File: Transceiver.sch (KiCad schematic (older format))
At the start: 31 parts

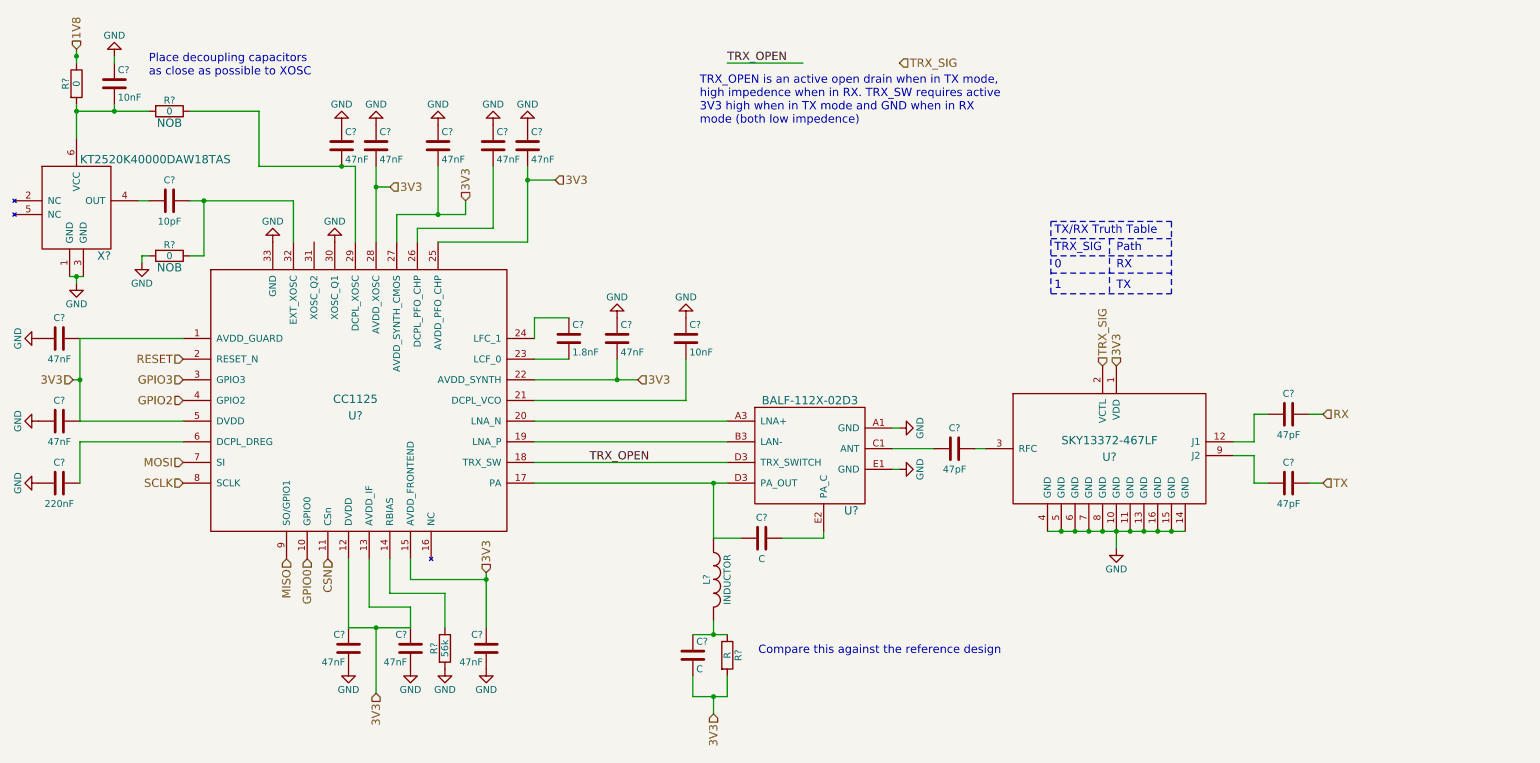
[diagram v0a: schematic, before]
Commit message: added jumpers for regulater EN and a jumper for fixing PA_ADJ. Connceted TRX_SIG to GPIO0
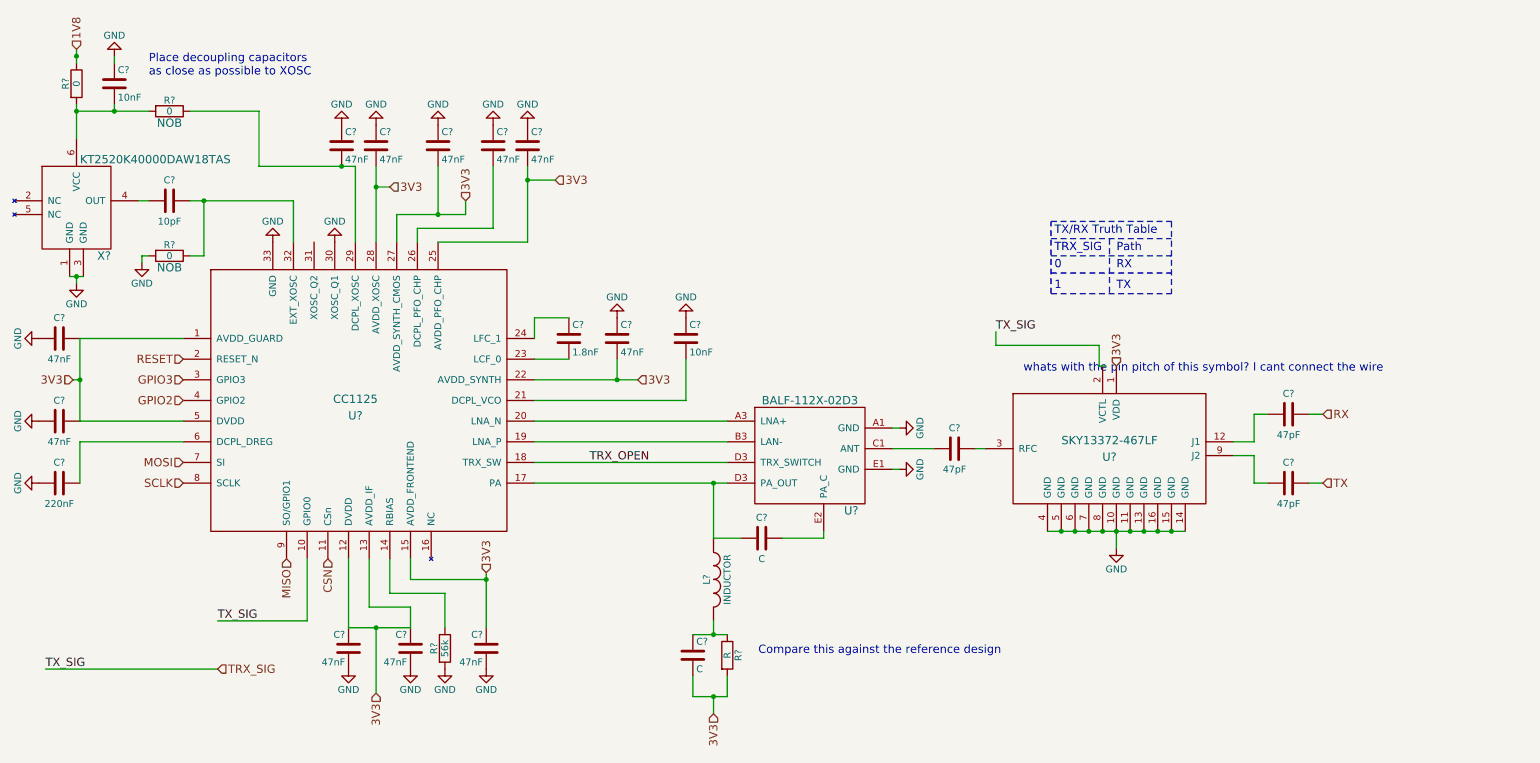
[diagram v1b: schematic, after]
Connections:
- net GPIO0 is gone; now on net TRX_SIG: U?.10 (GPIO0)
- net TRX_SIG: no longer U?.2 (VCTL)
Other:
- note added: "whats with the pin pitch of this symbol? I cant connect the wire\n"
- note removed: "TRX_OPEN is an active open drain when in TX mode, \nhigh impedence when in RX. TRX_SW requires active \n3V3 high when in TX mode and GND when in RX \nmode (both low impedence)"
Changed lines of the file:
@@
 Text HLabel 2550 4600 3    60   Input ~ 0
 MISO
-Text HLabel 2700 4600 3    60   Input ~ 0
-GPIO0
 Text HLabel 2850 4600 3    60   Input ~ 0
 CSN
@@
 Text HLabel 4500 1850 2    60   Input ~ 0
 3V3
-Text HLabel 7000 1000 2    60   Input ~ 0
+Text HLabel 2050 5400 2    60   Input ~ 0
 TRX_SIG
 $Comp
@@
 Text Label 4750 3900 0    60   ~ 0
 TRX_OPEN
-Text Label 5750 1000 0    60   ~ 0
-TRX_OPEN
+Text Label 800  5400 0    60   ~ 0
+TX_SIG
 Text HLabel 5650 5725 3    60   Input ~ 0
 3V3
-Text Notes 5550 1450 0    60   ~ 0
-TRX_OPEN is an active open drain when in TX mode, \nhigh impedence when in RX. TRX_SW requires active \n3V3 high when in TX mode and GND when in RX \nmode (both low impedence)
 Text Notes 1550 1100 0    60   ~ 0
 Place decoupling capacitors\nas close as possible to XOSC\n
@@
 	0    1    1    0
 $EndComp
-Text HLabel 8475 3200 1    60   Input ~ 0
-TRX_SIG
 Text Notes 8125 2375 0    60   ~ 0
 TRX_SIG
@@
 Connection ~ 3200 5100
 Wire Wire Line
-	5750 1000 6300 1000
+	800  5400 2050 5400
 Wire Wire Line
 	5750 5600 5750 5450
@@
 Wire Wire Line
 	2350 1350 1850 1350
+Wire Wire Line
+	2700 4600 2700 5050
+Wire Wire Line
+	2700 5050 2050 5050
+Text Label 2050 5050 0    60   ~ 0
+TX_SIG
+Text Label 7700 2950 0    60   ~ 0
+TX_SIG
+Wire Wire Line
+	8500 3200 8450 3200
+Wire Wire Line
+	8450 3200 8450 3050
+Wire Wire Line
+	8450 3050 7700 3050
+Wire Wire Line
+	7700 3050 7700 2950
+Text Notes 7900 3250 0    60   ~ 0
+whats with the pin pitch of this symbol? I cant connect the wire\n
 $EndSCHEMATC

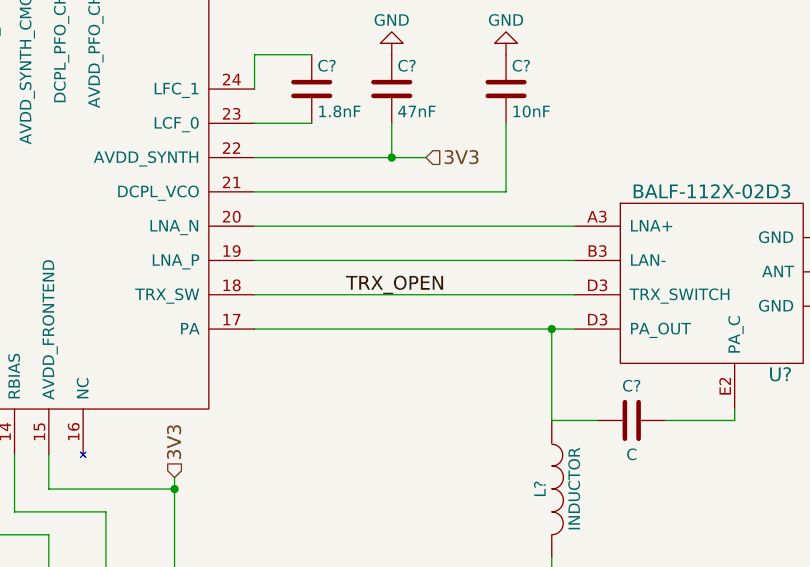
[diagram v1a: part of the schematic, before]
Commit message: deleted TRX_OPEN net
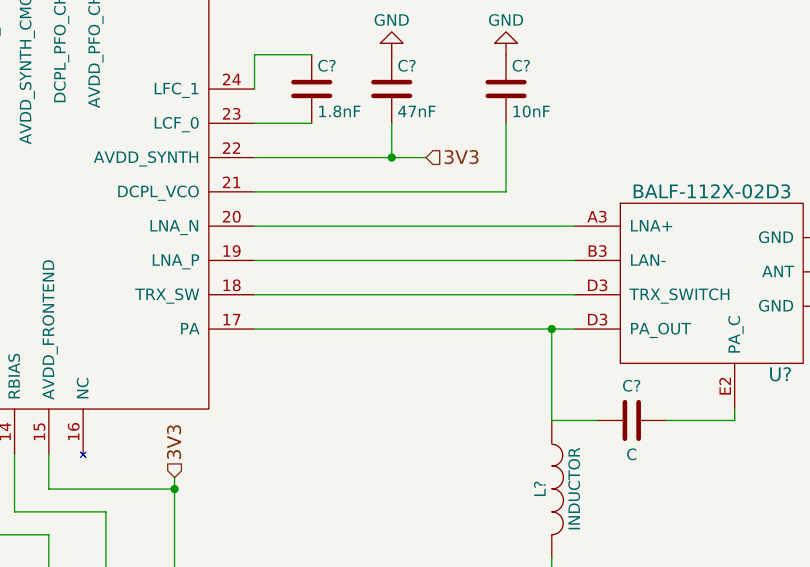
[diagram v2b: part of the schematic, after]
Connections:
- net TRX_OPEN: no longer names the net of U?.18 (TRX_SW), U?.D3 (TRX_SWITCH)
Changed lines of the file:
@@
 Text HLabel 5100 3300 2    60   Input ~ 0
 3V3
-Text Label 4750 3900 0    60   ~ 0
-TRX_OPEN
 Text Label 800  5400 0    60   ~ 0
 TX_SIG

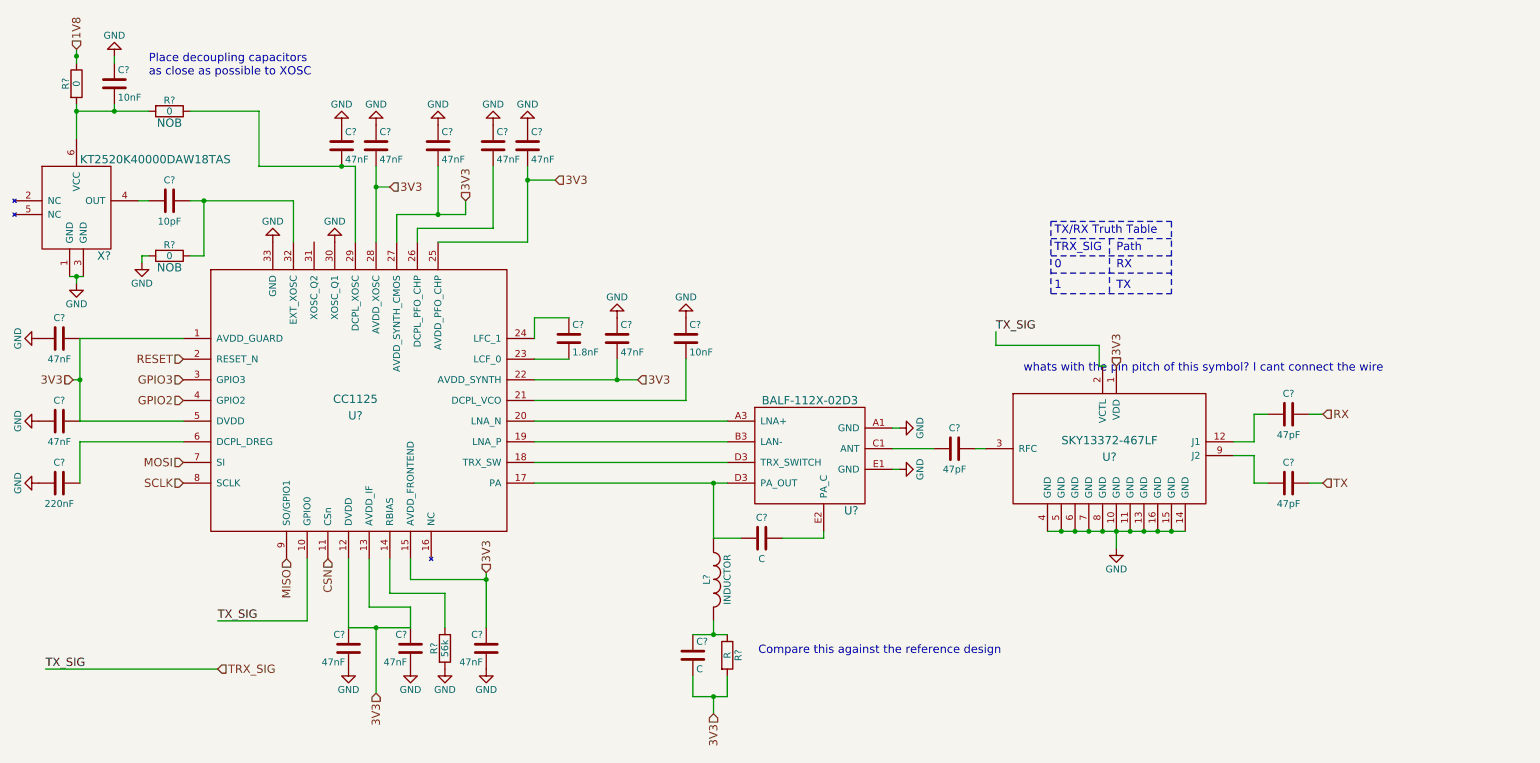
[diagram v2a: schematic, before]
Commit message: Added schematic of RT9183HGM5 (TO263-5)
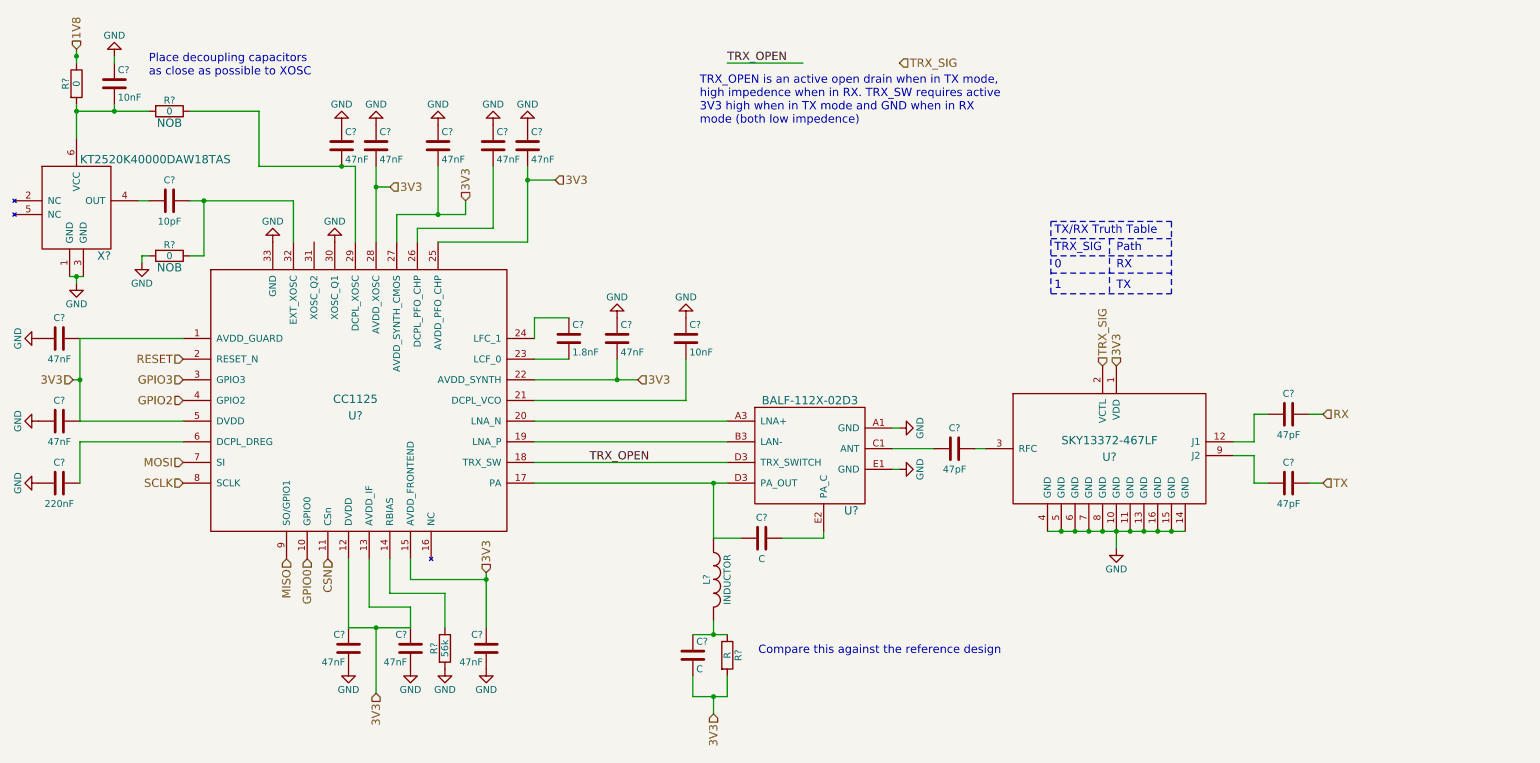
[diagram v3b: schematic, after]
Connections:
- net TRX_SIG: now also U?.2 (VCTL); no longer U?.10 (GPIO0)
- net TRX_OPEN: now reaches U?.18 (TRX_SW), U?.D3 (TRX_SWITCH)
- new net GPIO0: U?.10 (GPIO0)
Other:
- note added: "TRX_OPEN is an active open drain when in TX mode, \nhigh impedence when in RX. TRX_SW requires active \n3V3 high when in TX mode and GND when in RX \nmode (both low impedence)"
- note removed: "whats with the pin pitch of this symbol? I cant connect the wire\n"
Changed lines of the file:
@@
 Text HLabel 2550 4600 3    60   Input ~ 0
 MISO
+Text HLabel 2700 4600 3    60   Input ~ 0
+GPIO0
 Text HLabel 2850 4600 3    60   Input ~ 0
 CSN
@@
 Text HLabel 4500 1850 2    60   Input ~ 0
 3V3
-Text HLabel 2050 5400 2    60   Input ~ 0
+Text HLabel 7000 1000 2    60   Input ~ 0
 TRX_SIG
 $Comp
@@
 Text HLabel 5100 3300 2    60   Input ~ 0
 3V3
-Text Label 800  5400 0    60   ~ 0
-TX_SIG
+Text Label 4750 3900 0    60   ~ 0
+TRX_OPEN
+Text Label 5750 1000 0    60   ~ 0
+TRX_OPEN
 Text HLabel 5650 5725 3    60   Input ~ 0
 3V3
+Text Notes 5550 1450 0    60   ~ 0
+TRX_OPEN is an active open drain when in TX mode, \nhigh impedence when in RX. TRX_SW requires active \n3V3 high when in TX mode and GND when in RX \nmode (both low impedence)
 Text Notes 1550 1100 0    60   ~ 0
 Place decoupling capacitors\nas close as possible to XOSC\n
@@
 	0    1    1    0
 $EndComp
+Text HLabel 8475 3200 1    60   Input ~ 0
+TRX_SIG
 Text Notes 8125 2375 0    60   ~ 0
 TRX_SIG
@@
 Connection ~ 3200 5100
 Wire Wire Line
-	800  5400 2050 5400
+	5750 1000 6300 1000
 Wire Wire Line
 	5750 5600 5750 5450
@@
 Wire Wire Line
 	2350 1350 1850 1350
-Wire Wire Line
-	2700 4600 2700 5050
-Wire Wire Line
-	2700 5050 2050 5050
-Text Label 2050 5050 0    60   ~ 0
-TX_SIG
-Text Label 7700 2950 0    60   ~ 0
-TX_SIG
-Wire Wire Line
-	8500 3200 8450 3200
-Wire Wire Line
-	8450 3200 8450 3050
-Wire Wire Line
-	8450 3050 7700 3050
-Wire Wire Line
-	7700 3050 7700 2950
-Text Notes 7900 3250 0    60   ~ 0
-whats with the pin pitch of this symbol? I cant connect the wire\n
 $EndSCHEMATC

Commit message: moved jumpers into respective schematics
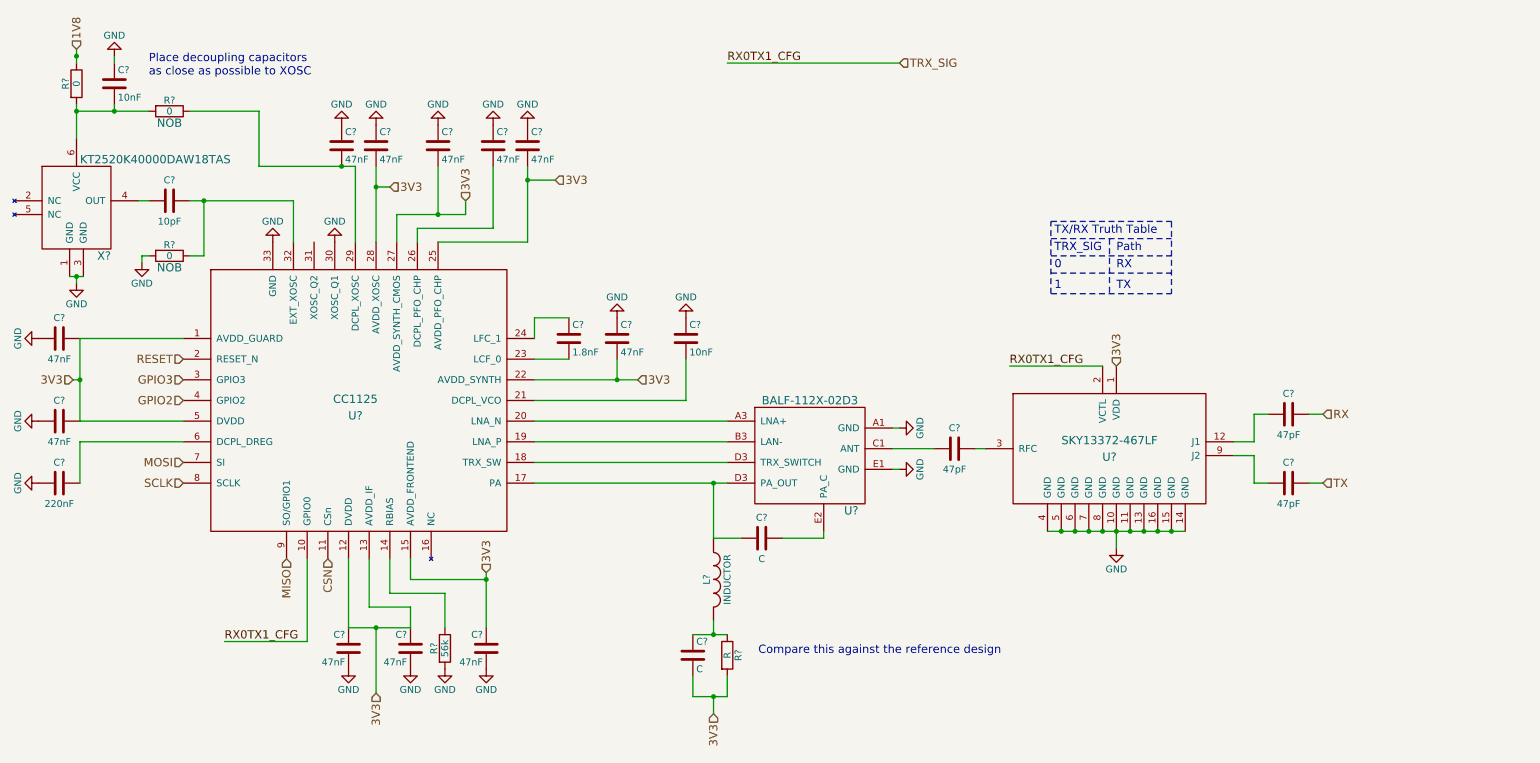
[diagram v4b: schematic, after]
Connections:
- net GPIO0 is gone; now on net TRX_SIG: U?.10 (GPIO0)
- net TRX_OPEN: no longer names the net of U?.18 (TRX_SW), U?.D3 (TRX_SWITCH)
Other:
- note removed: "TRX_OPEN is an active open drain when in TX mode, \nhigh impedence when in RX. TRX_SW requires active \n3V3 high when in TX mode and GND when in RX \nmode (both low impedence)"
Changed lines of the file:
@@
 Text HLabel 2550 4600 3    60   Input ~ 0
 MISO
-Text HLabel 2700 4600 3    60   Input ~ 0
-GPIO0
 Text HLabel 2850 4600 3    60   Input ~ 0
 CSN
@@
 Text HLabel 5100 3300 2    60   Input ~ 0
 3V3
-Text Label 4750 3900 0    60   ~ 0
-TRX_OPEN
-Text Label 5750 1000 0    60   ~ 0
-TRX_OPEN
 Text HLabel 5650 5725 3    60   Input ~ 0
 3V3
-Text Notes 5550 1450 0    60   ~ 0
-TRX_OPEN is an active open drain when in TX mode, \nhigh impedence when in RX. TRX_SW requires active \n3V3 high when in TX mode and GND when in RX \nmode (both low impedence)
 Text Notes 1550 1100 0    60   ~ 0
 Place decoupling capacitors\nas close as possible to XOSC\n
@@
 	0    1    1    0
 $EndComp
-Text HLabel 8475 3200 1    60   Input ~ 0
-TRX_SIG
 Text Notes 8125 2375 0    60   ~ 0
 TRX_SIG
@@
 Connection ~ 3200 5100
 Wire Wire Line
-	5750 1000 6300 1000
+	5750 1000 7000 1000
 Wire Wire Line
 	5750 5600 5750 5450
@@
 Wire Wire Line
 	2350 1350 1850 1350
+Wire Wire Line
+	2700 4600 2700 5200
+Wire Wire Line
+	2700 5200 2100 5200
+Text Label 2100 5200 0    60   ~ 0
+RX0TX1_CFG
+Text Label 5750 1000 0    60   ~ 0
+RX0TX1_CFG
+Wire Wire Line
+	7800 3200 8475 3200
+Text Label 7800 3200 0    60   ~ 0
+RX0TX1_CFG
 $EndSCHEMATC
